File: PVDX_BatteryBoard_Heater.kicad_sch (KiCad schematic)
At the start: 6 parts, among them Q3 PMOS, Q4 NMOS

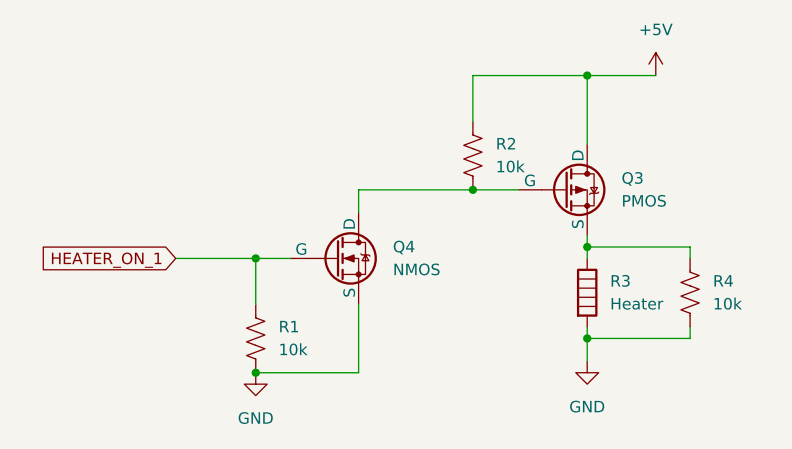
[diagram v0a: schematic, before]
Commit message: added second heater to heater schematic
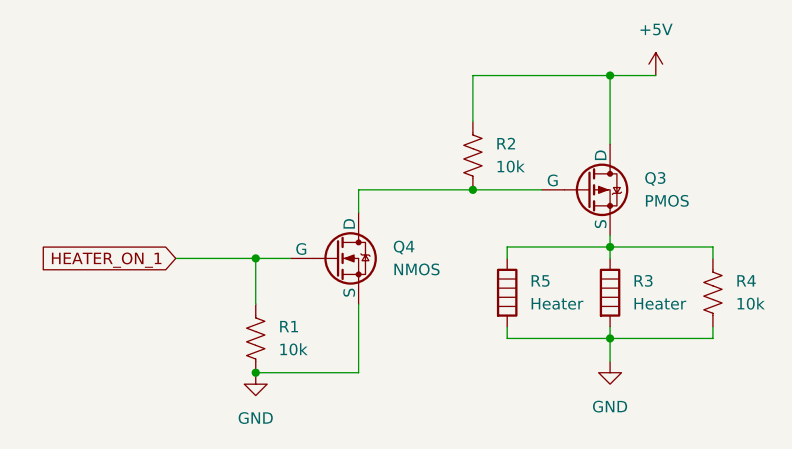
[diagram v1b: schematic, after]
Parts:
- added R5: Heater, symbol Device:Heater
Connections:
- net GND: now also R5.2
- net at Q3.3 (S), R3.1, R4.1: now also R5.1
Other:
- moved on the sheet: Q3, R3, R4
